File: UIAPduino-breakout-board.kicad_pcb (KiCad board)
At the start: 2 copper layers, 5 parts, among them J1 Conn_01x20_Pin, J2 Conn_01x20_Socket

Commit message: だいたい仕上げた
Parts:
- moved J1 8.89 mm to (181.6, 67.3)
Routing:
- net Net-(J1-Pin_18): track 25.2 -> 35.3 mm
- net Net-(J1-Pin_9): track 12.5 -> 22.6 mm
- net Net-(J1-Pin_8): track 12.5 -> 22.6 mm
- net Net-(J1-Pin_7): track 18.6 -> 28.8 mm
- net Net-(J1-Pin_20): track 50.9 -> 61.1 mm
- net Net-(J1-Pin_19): track 54.2 -> 64.3 mm
- net Net-(J1-Pin_17): track 45.1 -> 55.2 mm
- net Net-(J1-Pin_16): track 37.9 -> 48.0 mm
- net Net-(J1-Pin_13): track 34.9 -> 45.1 mm
- net Net-(J1-Pin_12): track 42.2 -> 52.4 mm
- net Net-(J1-Pin_11): track 41.5 -> 51.6 mm
- net Net-(J1-Pin_10): track 29.8 -> 40.0 mm
- net Net-(J1-Pin_14): track 30.3 -> 40.4 mm
- net Net-(J1-Pin_15): track 41.5 -> 51.6 mm
- added copper zone on B.Cu, net +5V
- added copper zone on B.Cu, net GND
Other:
- board outline added: 55.9 x 55.9 mm
- board text added: "*2"
- board text added: "*5"
- board text added: "*6/A2"
- board text added: "0/A1"
- board text added: "1/A0"
- board text added: "10"
- board text added: "11"
- board text added: "12/A3"
- board text added: "3.3V"
- board text added: "3/SDA"
- board text added: "4/SCL"
- board text added: "5V"
- board text added: "7/SCK"
- board text added: "8/MOSI"
- board text added: "9/MISO"
- board text added: "GND"
- board text added: "UIAPduino Breakout Board v1 https://github.com/53175ddd"
- board text added: "~{RESET}"

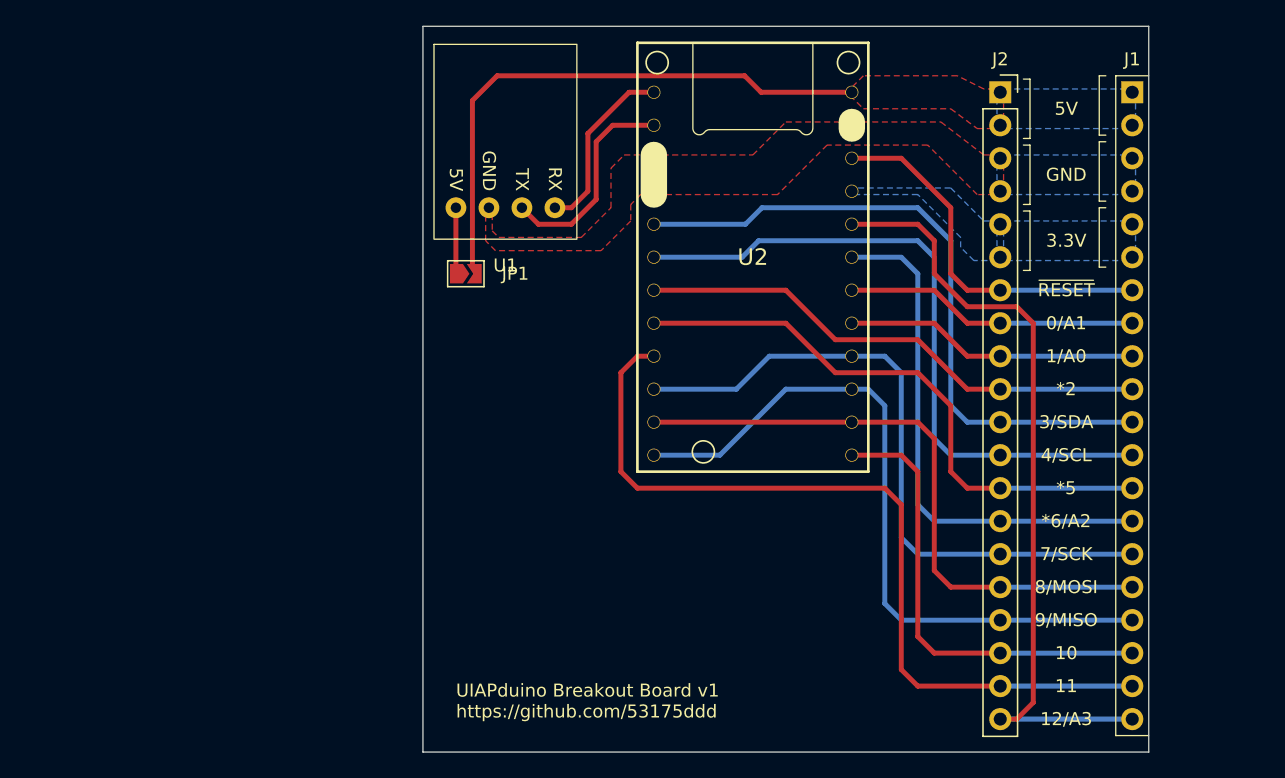
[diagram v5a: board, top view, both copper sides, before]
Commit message: JP の向きを反転
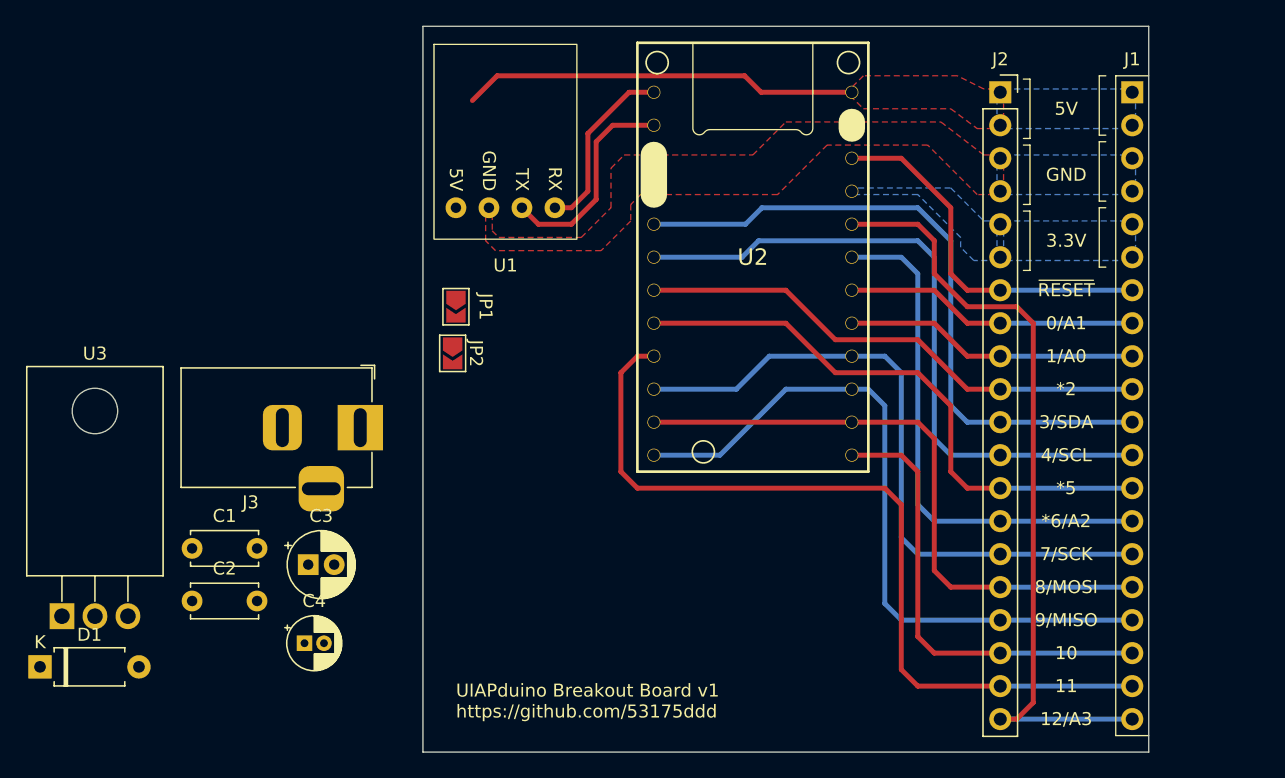
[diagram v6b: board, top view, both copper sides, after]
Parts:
- added C1: 0.22u, Capacitor_THT:C_Disc_D5.0mm_W2.5mm_P5.00mm, F.Cu at (109.2, 102.4)
- added C2: 0.1u, Capacitor_THT:C_Disc_D5.0mm_W2.5mm_P5.00mm, F.Cu at (109.2, 106.5)
- added C3: 47u, Capacitor_THT:CP_Radial_D5.0mm_P2.00mm, F.Cu at (118.2, 103.7)
- added C4: 10u, Capacitor_THT:CP_Radial_D4.0mm_P1.50mm, F.Cu at (117.9, 109.7)
- added D1: D, Diode_THT:D_A-405_P7.62mm_Horizontal, F.Cu at (97.5, 111.5)
- added J3: Barrel_Jack_Switch, Connector_BarrelJack:BarrelJack_Horizontal, F.Cu at (122.2, 93.1)
- added JP2: Jumper_2_Open, Jumper:SolderJumper-2_P1.3mm_Open_TrianglePad1.0x1.5mm, F.Cu at (129.3, 87.4)
- added U3: L7805, Package_TO_SOT_THT:TO-220F-3_Horizontal_TabDown, F.Cu at (99.2, 107.6)
- moved JP1 2.65 mm to (129.5, 83.8), turned to -90 degrees
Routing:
- net +5V: track 43.7 -> 30.5 mm
- net Net-(JP1-A): track 5.08 -> 0.00 mm

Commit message: 電源回路追加
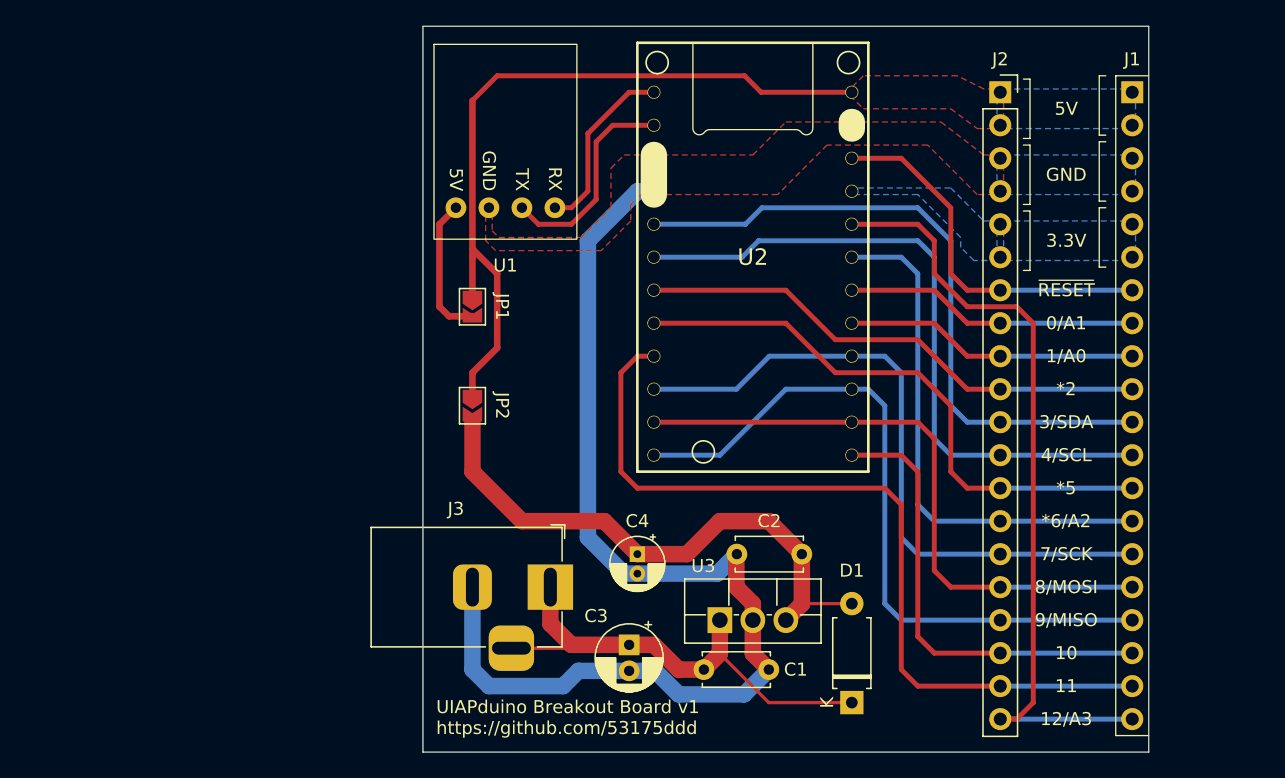
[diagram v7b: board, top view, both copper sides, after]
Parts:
- U3: footprint Package_TO_SOT_THT:TO-220F-3_Horizontal_TabDown -> Package_TO_SOT_THT:TO-220F-3_Vertical
- moved D1 62.6 mm to (160.0, 114.3), turned to 90 degrees
- moved U3 50.7 mm to (149.9, 108.0)
- moved C2 47.1 mm to (156.2, 102.9), turned to 180 degrees
- moved C1 40.5 mm to (148.6, 111.8)
- moved C4 26.5 mm to (143.5, 102.9), turned to -90 degrees
- moved C3 25.5 mm to (142.9, 109.9), turned to -90 degrees
- moved J3 19.1 mm to (136.8, 105.4)
- moved JP2 4.31 mm to (130.8, 91.4)
- moved JP1 1.27 mm to (130.8, 83.8)
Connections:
- JP1 pad 1: Net-(JP1-A) -> +5V
- JP1 pad 2: +5V -> Net-(JP1-B)
- JP2 pad 1: Net-(D1-A) -> +5V
- JP2 pad 2: +5V -> Net-(D1-A)
- U1 pad 1: Net-(JP1-A) -> Net-(JP1-B)
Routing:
- net GND: track 0.00 -> 84.4 mm
- net Net-(D1-A): track 0.00 -> 43.4 mm
- net +12V: track 0.00 -> 36.9 mm
- net +5V: track 30.5 -> 58.6 mm
- net Net-(JP1-B): track 0.00 -> 11.0 mm

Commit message: 外形とシルクを調整
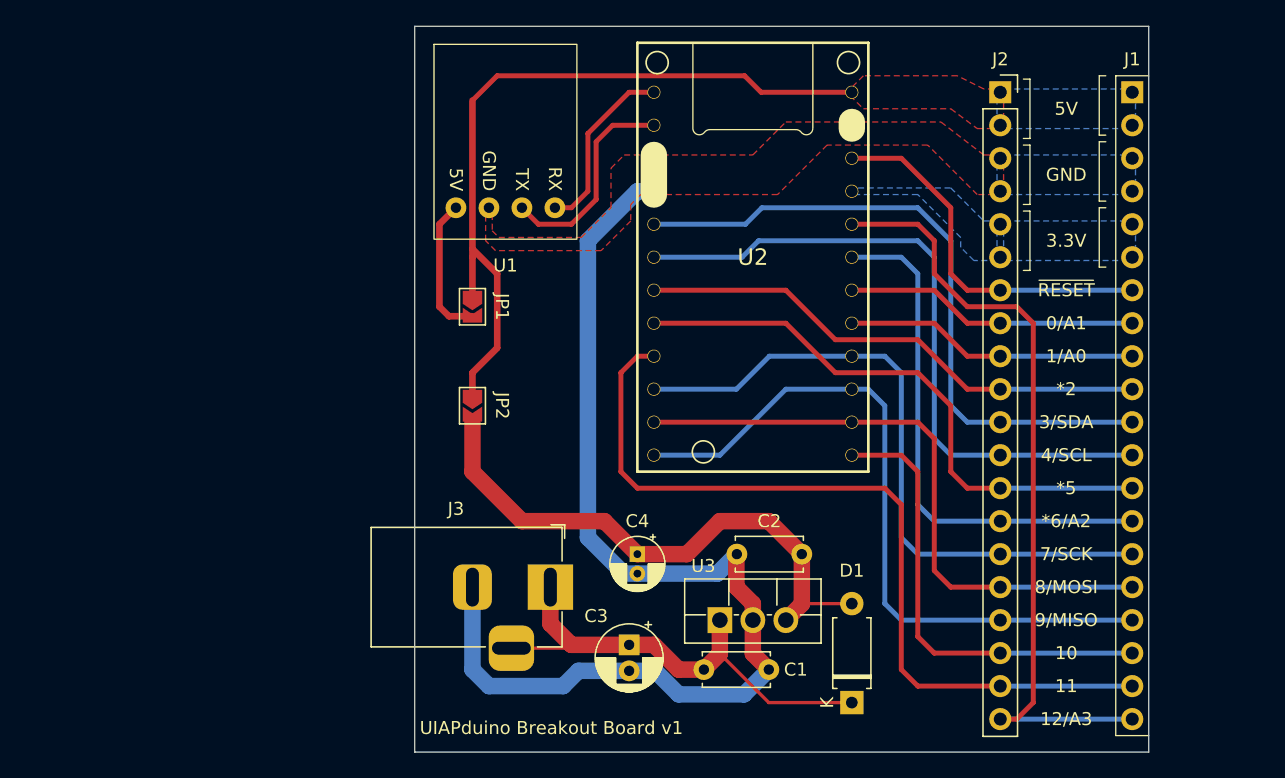
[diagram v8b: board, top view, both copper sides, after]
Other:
- board size 55.9 x 55.9 mm -> 56.5 x 55.9 mm
- board text added: "UIAPduino Breakout Board v1"
- board text added: "https://github.com/53175ddd/UIAPduino-breakout-board"
- board text removed: "UIAPduino Breakout Board v1 https://github.com/53175ddd"
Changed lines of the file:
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@@
 		(tags "TO-220F-3 Vertical RM 2.54mm")
 		(property "Reference" "U3"
-			(at -1.27 -4.1675 360)
+			(at -1.27 -4.1675 0)
 			(layer "F.SilkS")
 			(effects
@@
 		)
 		(property "Value" "L7805"
-			(at 2.54 2.9025 360)
+			(at 2.54 2.9025 0)
 			(layer "F.Fab")
 			(effects
@@
 		)
 		(fp_text user "${REFERENCE}"
-			(at 2.54 -4.1675 360)
+			(at 2.54 -4.1675 0)
 			(layer "F.Fab")
 			(effects
@@
 		(tags "CP Radial series Radial pin pitch 2.00mm  diameter 5mm Electrolytic Capacitor")
 		(property "Reference" "C3"
-			(at -2.219888 2.54 360)
+			(at -2.219888 2.54 0)
 			(layer "F.SilkS")
 			(effects
@@
 		)
 		(property "Value" "0.22u"
-			(at 2.5 2.5 360)
+			(at 2.5 2.5 0)
 			(layer "F.Fab")
 			(effects
@@
 		)
 		(fp_text user "${REFERENCE}"
-			(at 2.5 0 360)
+			(at 2.5 0 0)
 			(layer "F.Fab")
 			(effects
@@
 		(tags "C Disc series Radial pin pitch 5.00mm  diameter 5mm width 2.5mm Capacitor")
 		(property "Reference" "C2"
-			(at 2.5 2.54 360)
+			(at 2.5 2.54 0)
 			(layer "F.SilkS")
 			(effects
@@
 		)
 		(property "Value" "0.1u"
-			(at 2.5 2.5 360)
+			(at 2.5 2.5 0)
 			(layer "F.Fab")
 			(effects
@@
 		)
 		(fp_text user "${REFERENCE}"
-			(at 2.5 0 360)
+			(at 2.5 0 0)
 			(layer "F.Fab")
 			(effects
@@
 		(tags "CP Radial series Radial pin pitch 1.50mm  diameter 4mm Electrolytic Capacitor")
 		(property "Reference" "C4"
-			(at -2.54 0 360)
+			(at -2.54 0 0)
 			(layer "F.SilkS")
 			(effects
@@
 		(tags "Through hole pin header THT 1x20 2.54mm single row")
 		(property "Reference" "J1"
-			(at 0 2.54 -0)
+			(at 0 2.54 0)
 			(layer "F.SilkS")
 			(effects
@@
 	)
 	(gr_rect
-		(start 127 62.23)
+		(start 126.365 62.23)
 		(end 182.88 118.11)
 		(stroke
@@
 		(layer "Edge.Cuts")
 	)
+	(gr_text "https://github.com/53175ddd/UIAPduino-breakout-board"
+		(at 127 116.84 -90)
+		(layer "B.SilkS")
+		(effects
+			(font
+				(size 1 1)
+				(thickness 0.1)
+			)
+			(justify left bottom mirror)
+		)
+	)
 	(gr_text "0/A1"
 		(at 176.53 85.09 0)
@@
 		)
 	)
-	(gr_text "UIAPduino Breakout Board v1\nhttps://github.com/53175ddd"
-		(at 128.016 116.84 0)
+	(gr_text "UIAPduino Breakout Board v1"
+		(at 126.746 116.84 0)
 		(layer "F.SilkS")
 		(effects
